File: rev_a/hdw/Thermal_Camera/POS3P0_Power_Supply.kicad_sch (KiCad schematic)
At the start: 24 parts

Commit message: lots of schematic progress
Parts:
- C401, C406: renamed from C?; footprint Capacitors_SMD:C_0603 -> (none); Digi-Key PN 1276-1935-1-ND -> (none); display_footprint 0603 -> (none)
- C403: renamed from C?; footprint Capacitors_SMD:C_0603 -> (none); Digi-Key PN 399-8153-1-ND -> (none); display_footprint 0603 -> (none)
- C405: renamed from C?; footprint Capacitors_SMD:C_0603 -> (none); Digi-Key PN 399-7842-1-ND -> (none); display_footprint 0603 -> (none)
- R401: renamed from R?; footprint Resistors_SMD:R_0603 -> (none); Digi-Key PN 541-2982-1-ND -> (none); Wattage 1/10W -> (none); display_footprint 0603 -> (none)
- R402, R403, R404: renamed from R?; footprint Resistors_SMD:R_0603 -> (none); Digi-Key PN 541-10.0KHCT-ND -> (none); Wattage 1/10W -> (none); display_footprint 0603 -> (none)
- R408, R409: renamed from R?; footprint Resistors_SMD:R_0603 -> (none); Wattage 1/10W -> (none); display_footprint 0603 -> (none)
- R? (x2): footprint Resistors_SMD:R_0603 -> (none); Digi-Key PN 541-10.0HCT-ND -> (none); Wattage 1/10W -> (none); display_footprint 0603 -> (none)
- gave numbers to parts that had none: 11

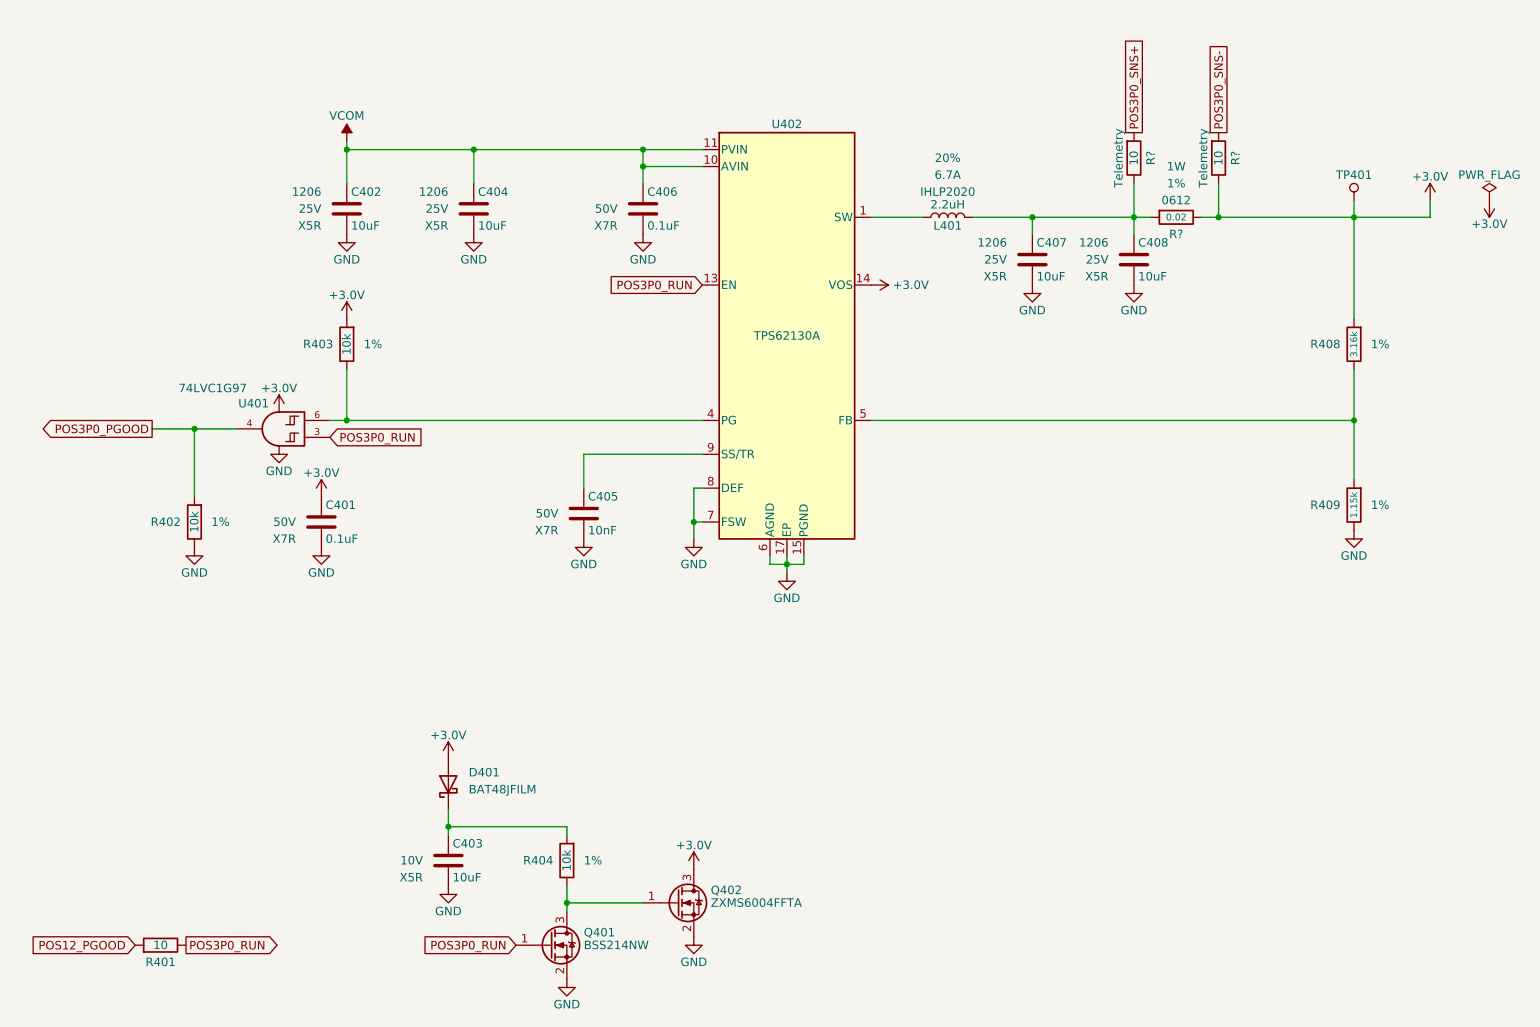
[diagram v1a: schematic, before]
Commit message: assigned a ton of footprints
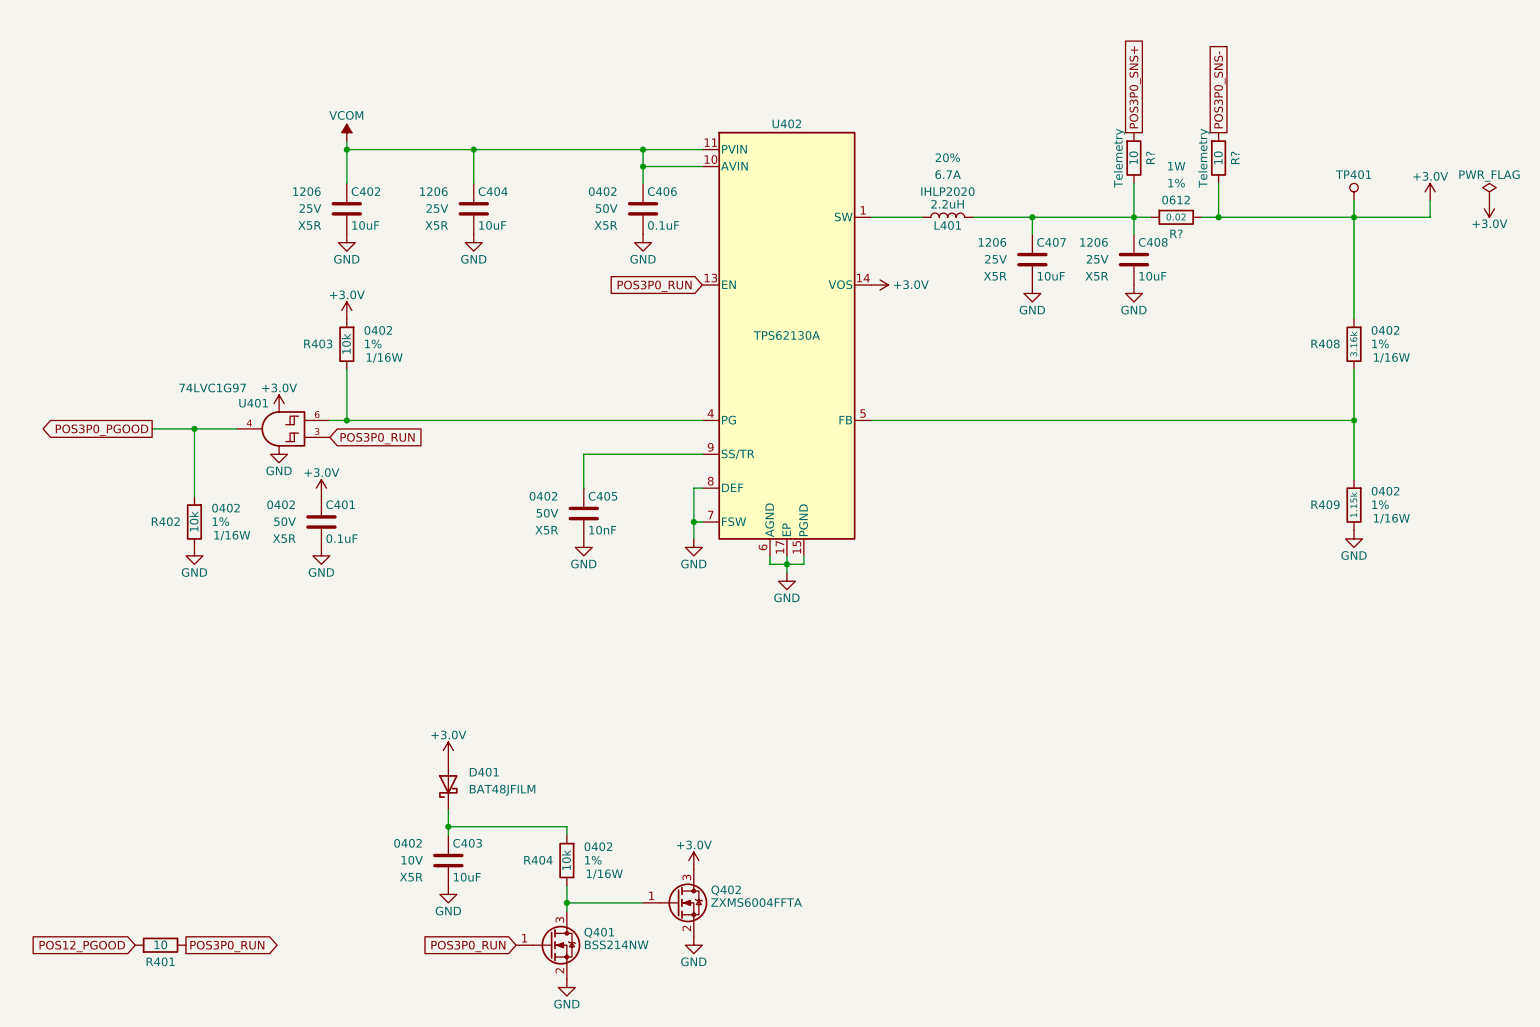
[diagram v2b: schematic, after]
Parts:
- C401, C405, C406: footprint (none) -> Capacitors_SMD:C_0402; Dielectric X7R -> X5R; display_footprint (none) -> 0402
- C403: footprint (none) -> Capacitors_SMD:C_0402; display_footprint (none) -> 0402
- R401, R402, R403, R404, R408, R409, R? (x2): footprint (none) -> Resistors_SMD:R_0402; Wattage (none) -> 1/16W; display_footprint (none) -> 0402
- U401: Digi-Key PN 1727-1772-1-ND -> 296-15582-1-ND
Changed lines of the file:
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@@
 			)
 		)
-		(property "Footprint" ""
+		(property "Footprint" "Resistors_SMD:R_0402"
 			(at 106.68 156.21 0)
 			(effects
@@
 			)
 		)
-		(property "display_footprint" ""
+		(property "display_footprint" "0402"
 			(at 109.22 154.178 0)
 			(effects
@@
 			)
 		)
-		(property "Wattage" ""
+		(property "Wattage" "1/16W"
 			(at 109.474 158.242 0)
 			(effects
@@
 			)
 		)
-		(property "Footprint" ""
+		(property "Footprint" "Capacitors_SMD:C_0402"
 			(at 110.1852 107.95 0)
 			(effects
@@
 			)
 		)
-		(property "display_footprint" ""
+		(property "display_footprint" "0402"
 			(at 105.41 101.6 0)
 			(effects
@@
 			)
 		)
-		(property "Dielectric" "X7R"
+		(property "Dielectric" "X5R"
 			(at 105.41 106.68 0)
 			(effects
@@
 			)
 		)
-		(property "Footprint" ""
+		(property "Footprint" "Resistors_SMD:R_0402"
 			(at 224.79 78.74 0)
 			(effects
@@
 			)
 		)
-		(property "display_footprint" ""
+		(property "display_footprint" "0402"
 			(at 227.33 76.708 0)
 			(effects
@@
 			)
 		)
-		(property "Wattage" ""
+		(property "Wattage" "1/16W"
 			(at 227.584 80.772 0)
 			(effects
@@
 			)
 		)
-		(property "Footprint" ""
+		(property "Footprint" "Resistors_SMD:R_0402"
 			(at 191.77 50.8 0)
 			(effects
@@
 			)
 		)
-		(property "display_footprint" ""
+		(property "display_footprint" "0402"
 			(at 189.23 50.8 90)
 			(effects
@@
 			)
 		)
-		(property "Wattage" ""
+		(property "Wattage" "1/16W"
 			(at 184.15 50.8 90)
 			(effects
@@
 			)
 		)
-		(property "Footprint" ""
+		(property "Footprint" "Resistors_SMD:R_0402"
 			(at 224.79 102.87 0)
 			(effects
@@
 			)
 		)
-		(property "display_footprint" ""
+		(property "display_footprint" "0402"
 			(at 227.33 100.838 0)
 			(effects
@@
 			)
 		)
-		(property "Wattage" ""
+		(property "Wattage" "1/16W"
 			(at 227.584 104.902 0)
 			(effects
@@
 			)
 		)
-		(property "Footprint" ""
+		(property "Footprint" "Capacitors_SMD:C_0402"
 			(at 70.8152 109.22 0)
 			(effects
@@
 			)
 		)
-		(property "display_footprint" ""
+		(property "display_footprint" "0402"
 			(at 66.04 102.87 0)
 			(effects
@@
 			)
 		)
-		(property "Dielectric" "X7R"
+		(property "Dielectric" "X5R"
 			(at 66.04 107.95 0)
 			(effects
@@
 			)
 		)
-		(property "Footprint" ""
+		(property "Footprint" "Capacitors_SMD:C_0402"
 			(at 89.8652 160.02 0)
 			(effects
@@
 			)
 		)
-		(property "display_footprint" ""
+		(property "display_footprint" "0402"
 			(at 85.09 153.67 0)
 			(effects
@@
 			)
 		)
-		(property "Digi-Key PN" "1727-1772-1-ND"
+		(property "Digi-Key PN" "296-15582-1-ND"
 			(at 63.5 91.44 0)
 			(effects
@@
 			)
 		)
-		(property "Footprint" ""
+		(property "Footprint" "Resistors_SMD:R_0402"
 			(at 50.8 105.41 0)
 			(effects
@@
 			)
 		)
-		(property "display_footprint" ""
+		(property "display_footprint" "0402"
 			(at 53.34 103.378 0)
 			(effects
@@
 			)
 		)
-		(property "Wattage" ""
+		(property "Wattage" "1/16W"
 			(at 53.594 107.442 0)
 			(effects
@@
 			)
 		)
-		(property "Footprint" ""
+		(property "Footprint" "Capacitors_SMD:C_0402"
 			(at 119.0752 62.23 0)
 			(effects
@@
 			)
 		)
-		(property "display_footprint" ""
+		(property "display_footprint" "0402"
 			(at 114.3 55.88 0)
 			(effects
@@
 			)
 		)
-		(property "Dielectric" "X7R"
+		(property "Dielectric" "X5R"
 			(at 114.3 60.96 0)
 			(effects
@@
 			)
 		)
-		(property "Footprint" ""
+		(property "Footprint" "Resistors_SMD:R_0402"
 			(at 73.66 78.74 0)
 			(effects
@@
 			)
 		)
-		(property "display_footprint" ""
+		(property "display_footprint" "0402"
 			(at 76.2 76.708 0)
 			(effects
@@
 			)
 		)
-		(property "Wattage" ""
+		(property "Wattage" "1/16W"
 			(at 76.454 80.772 0)
 			(effects
@@
 			)
 		)
-		(property "Footprint" ""
+		(property "Footprint" "Resistors_SMD:R_0402"
 			(at 204.47 50.8 0)
 			(effects
@@
 			)
 		)
-		(property "display_footprint" ""
+		(property "display_footprint" "0402"
 			(at 201.93 50.8 90)
 			(effects
@@
 			)
 		)
-		(property "Wattage" ""
+		(property "Wattage" "1/16W"
 			(at 196.85 50.8 90)
 			(effects
@@
 			)
 		)
-		(property "Footprint" ""
+		(property "Footprint" "Resistors_SMD:R_0402"
 			(at 45.72 168.91 0)
 			(effects
@@
 			)
 		)
-		(property "display_footprint" ""
+		(property "display_footprint" "0402"
 			(at 43.434 166.37 0)
 			(effects
@@
 			)
 		)
-		(property "Wattage" ""
+		(property "Wattage" "1/16W"
 			(at 48.26 166.37 0)
 			(effects

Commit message: assigned some part numbers
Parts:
- C401, C406: Digi-Key PN (none) -> 490-10697-1-ND
- C403: Digi-Key PN (none) -> 490-GRM155R61A106ME11DCT-ND
- C405: Digi-Key PN (none) -> 445-12201-1-ND
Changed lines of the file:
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@@
 			)
 		)
-		(property "Digi-Key PN" ""
+		(property "Digi-Key PN" "445-12201-1-ND"
 			(at 109.22 104.14 0)
 			(effects
@@
 			)
 		)
-		(property "Digi-Key PN" ""
+		(property "Digi-Key PN" "490-10697-1-ND"
 			(at 69.85 105.41 0)
 			(effects
@@
 			)
 		)
-		(property "Digi-Key PN" ""
+		(property "Digi-Key PN" "490-GRM155R61A106ME11DCT-ND"
 			(at 88.9 156.21 0)
 			(effects
@@
 			)
 		)
-		(property "Digi-Key PN" ""
+		(property "Digi-Key PN" "490-10697-1-ND"
 			(at 118.11 58.42 0)
 			(effects

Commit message: assigned resistor part numbers
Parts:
- R401, R? (x2): Digi-Key PN (none) -> RMCF0402FT10R0CT-ND
- R402, R403, R404: Digi-Key PN (none) -> RMCF0402FT10K0CT-ND
- R408: Digi-Key PN (none) -> RMCF0402FT3K16CT-ND
- R409: Digi-Key PN (none) -> RMCF0402FT1K15CT-ND
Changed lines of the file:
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@@
 			)
 		)
-		(property "Digi-Key PN" ""
+		(property "Digi-Key PN" "RMCF0402FT10K0CT-ND"
 			(at 114.3 146.05 0)
 			(effects
@@
 			)
 		)
-		(property "Digi-Key PN" ""
+		(property "Digi-Key PN" "RMCF0402FT3K16CT-ND"
 			(at 224.79 78.74 0)
 			(effects
@@
 			)
 		)
-		(property "Digi-Key PN" ""
+		(property "Digi-Key PN" "RMCF0402FT10R0CT-ND"
 			(at 191.77 50.8 0)
 			(effects
@@
 			)
 		)
-		(property "Digi-Key PN" ""
+		(property "Digi-Key PN" "RMCF0402FT1K15CT-ND"
 			(at 224.79 102.87 0)
 			(effects
@@
 			)
 		)
-		(property "Digi-Key PN" ""
+		(property "Digi-Key PN" "RMCF0402FT10K0CT-ND"
 			(at 58.42 95.25 0)
 			(effects
@@
 			)
 		)
-		(property "Digi-Key PN" ""
+		(property "Digi-Key PN" "RMCF0402FT10K0CT-ND"
 			(at 81.28 68.58 0)
 			(effects
@@
 			)
 		)
-		(property "Digi-Key PN" ""
+		(property "Digi-Key PN" "RMCF0402FT10R0CT-ND"
 			(at 204.47 50.8 0)
 			(effects
@@
 			)
 		)
-		(property "Digi-Key PN" ""
+		(property "Digi-Key PN" "RMCF0402FT10R0CT-ND"
 			(at 45.72 168.91 0)
 			(effects
